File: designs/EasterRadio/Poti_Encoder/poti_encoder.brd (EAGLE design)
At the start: 50 x 33 mm, 12 parts

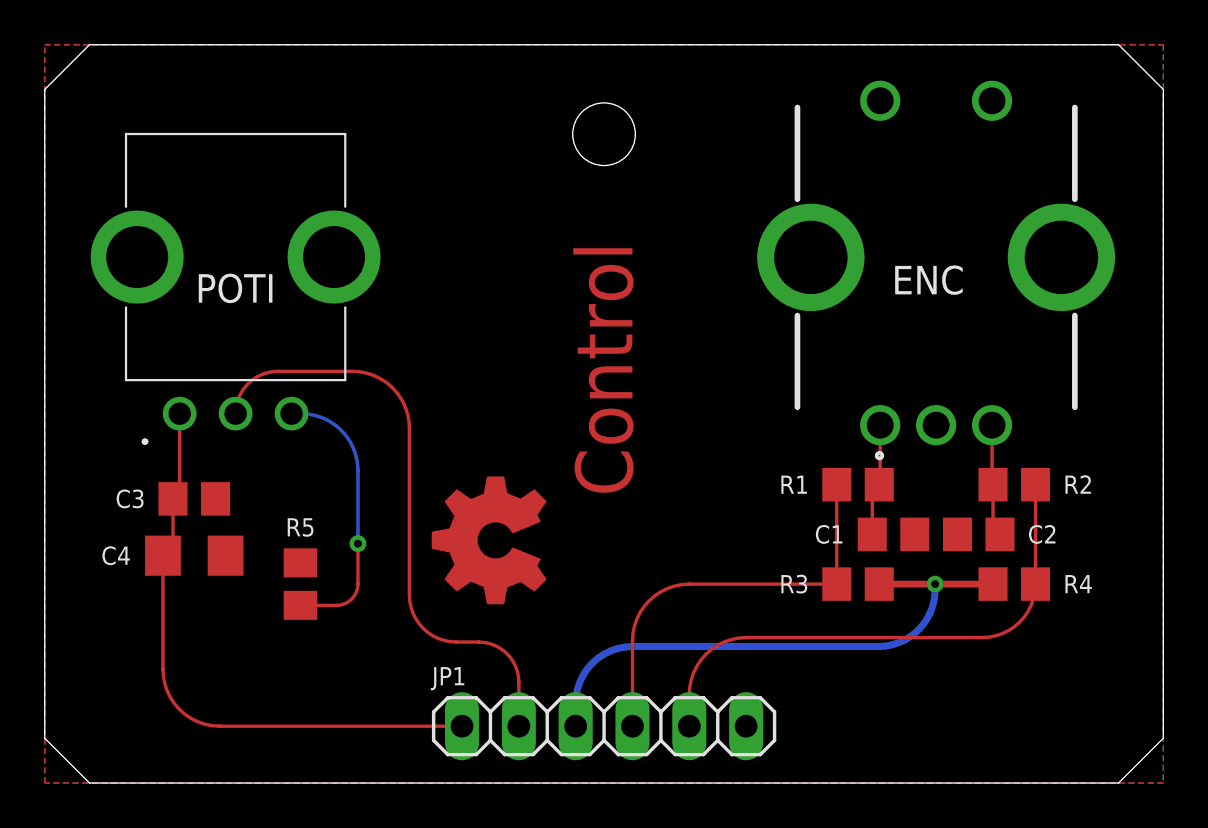
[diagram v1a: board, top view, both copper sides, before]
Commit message: added esd for rs232 to can
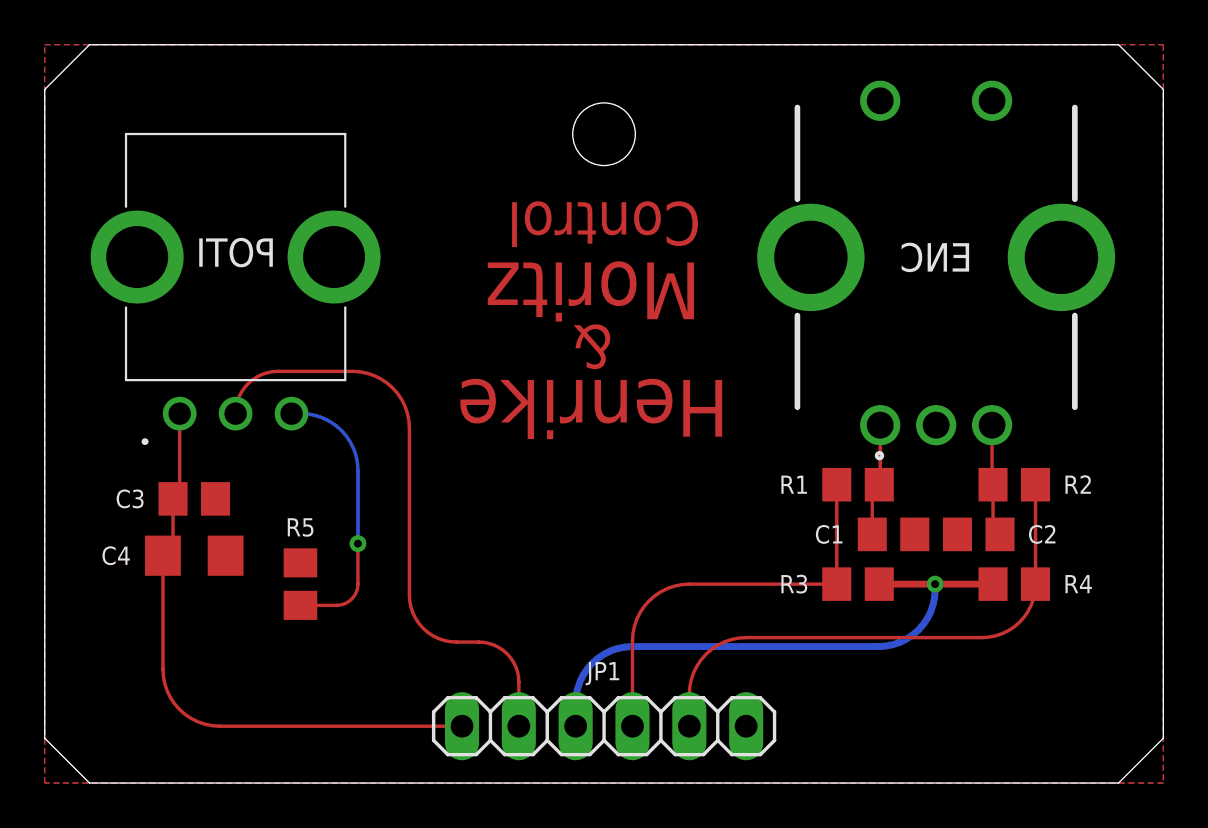
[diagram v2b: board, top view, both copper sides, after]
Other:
- board text added: "&"
- board text added: "Henrike"
- board text added: "Moritz"

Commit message: added mainboard layout and new 3.5mm jack
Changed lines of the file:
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@@
 <drawing>
 <settings>
-<setting alwaysvectorfont="yes"/>
+<setting alwaysvectorfont="no"/>
 <setting verticaltext="up"/>
 </settings>
-<grid distance="0.1" unitdist="mm" unit="mm" style="lines" multiple="1" display="yes" altdistance="5" altunitdist="mil" altunit="mil"/>
+<grid distance="1" unitdist="mm" unit="mm" style="lines" multiple="1" display="yes" altdistance="5" altunitdist="mil" altunit="mil"/>
 <layers>
 <layer number="1" name="Top" color="4" fill="1" visible="yes" active="yes"/>
@@
 </layers>
 <board>
-<fusionsync huburn="a.cGVyc29uYWw6dWUyYTNmMDU1" projecturn="a.cGVyc29uYWw6dWUyYTNmMDU1IzIwMTgxMjEwMTY0OTQ5MjI2" f3durn="urn:adsk.wipprod:dm.lineage:M7AeiVjzTJGZoft4LL6nBQ" pcbguid="" lastpulledtime="" lastsyncedchangeguid="" latestrevisionid="d82b5e06-51e9-49e7-8f0b-4ea682529d46" lastsyncedrevisionid="d82b5e06-51e9-49e7-8f0b-4ea682529d46" lastboardhashguid="21f51aed-d76b-e7f7-df56-29353063c362" lastpushedtime="2020-11-29T20:54:37Z" linktopcb3d="true"/>
+<fusionsync huburn="a.cGVyc29uYWw6dWUyYTNmMDU1" projecturn="a.cGVyc29uYWw6dWUyYTNmMDU1IzIwMTgxMjEwMTY0OTQ5MjI2" f3durn="urn:adsk.wipprod:dm.lineage:M7AeiVjzTJGZoft4LL6nBQ" pcbguid="" lastpulledtime="" lastsyncedchangeguid="" latestrevisionid="cf63cf35-bc2a-43f9-a261-0c7b6653c30b" lastsyncedrevisionid="cf63cf35-bc2a-43f9-a261-0c7b6653c30b" lastboardhashguid="2272ed55-4336-9e6e-18f4-f478c56222c7" lastpushedtime="2020-12-06T22:16:45Z" linktopcb3d="true"/>
 <plain>
 <hole x="25" y="29" drill="2.8"/>
@@
 <wire x1="0" y1="31" x2="2" y2="33" width="0" layer="20"/>
 <circle x="25" y="29" radius="1.4142125" width="2.54" layer="41"/>
-<text x="25" y="25" size="1.9304" layer="1" font="vector" ratio="15" rot="SR180" align="center">Control</text>
-<text x="25" y="25" size="1.9304" layer="29" font="vector" ratio="15" rot="SR180" align="center">Control</text>
-<text x="24.5" y="16.75" size="2.54" layer="29" font="vector" ratio="15" rot="SR180" align="center">Henrike</text>
-<text x="24.5" y="22" size="2.54" layer="29" font="vector" ratio="15" rot="SR180" align="center">Moritz</text>
-<text x="24.5" y="22" size="2.54" layer="1" font="vector" ratio="15" rot="SR180" align="center">Moritz</text>
-<text x="24.5" y="16.75" size="2.54" layer="1" font="vector" ratio="15" rot="SR180" align="center">Henrike</text>
-<text x="24.5" y="19.5" size="1.9304" layer="29" font="vector" ratio="15" rot="SR180" align="center">&amp;</text>
-<text x="24.5" y="19.5" size="1.9304" layer="1" font="vector" ratio="15" rot="SR180" align="center">&amp;</text>
+<text x="24.500003125" y="24.6" size="1.778" layer="1" font="vector" ratio="15" rot="SR180" align="center">Control</text>
+<text x="24.500003125" y="24.6" size="1.778" layer="29" font="vector" ratio="15" rot="SR180" align="center">Control</text>
+<text x="24.5" y="16.35" size="2.54" layer="29" font="vector" ratio="15" rot="SR180" align="center">Henrike</text>
+<text x="24.5" y="21.6" size="2.54" layer="29" font="vector" ratio="15" rot="SR180" align="center">Moritz</text>
+<text x="24.5" y="21.6" size="2.54" layer="1" font="vector" ratio="15" rot="SR180" align="center">Moritz</text>
+<text x="24.5" y="16.35" size="2.54" layer="1" font="vector" ratio="15" rot="SR180" align="center">Henrike</text>
+<text x="24.500003125" y="19.1" size="1.9304" layer="29" font="vector" ratio="15" rot="SR180" align="center">&amp;</text>
+<text x="24.500003125" y="19.1" size="1.9304" layer="1" font="vector" ratio="15" rot="SR180" align="center">&amp;</text>
+<hole x="47" y="3" drill="2.8"/>
+<circle x="47" y="3" radius="1.4142125" width="2.54" layer="41"/>
+<hole x="3" y="3" drill="2.8"/>
+<circle x="3" y="3" radius="1.4142125" width="2.54" layer="41"/>
 </plain>
 <attributes>
